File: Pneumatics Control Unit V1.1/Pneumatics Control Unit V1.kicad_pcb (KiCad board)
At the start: 4 copper layers, 53.6 x 65.4 mm, 80 parts, among them J1 TX_PORT, J10 Conn_01x02_Male, J11 Conn_01x02_Male, J12 10118194-0001LF, J13 Conn_01x03_Male, J14 Conn_01x03_Male, J2 RX_PORT, J3 MICROMOD-2222, J4 Conn_01x02_Male, J5 Conn_01x02_Male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

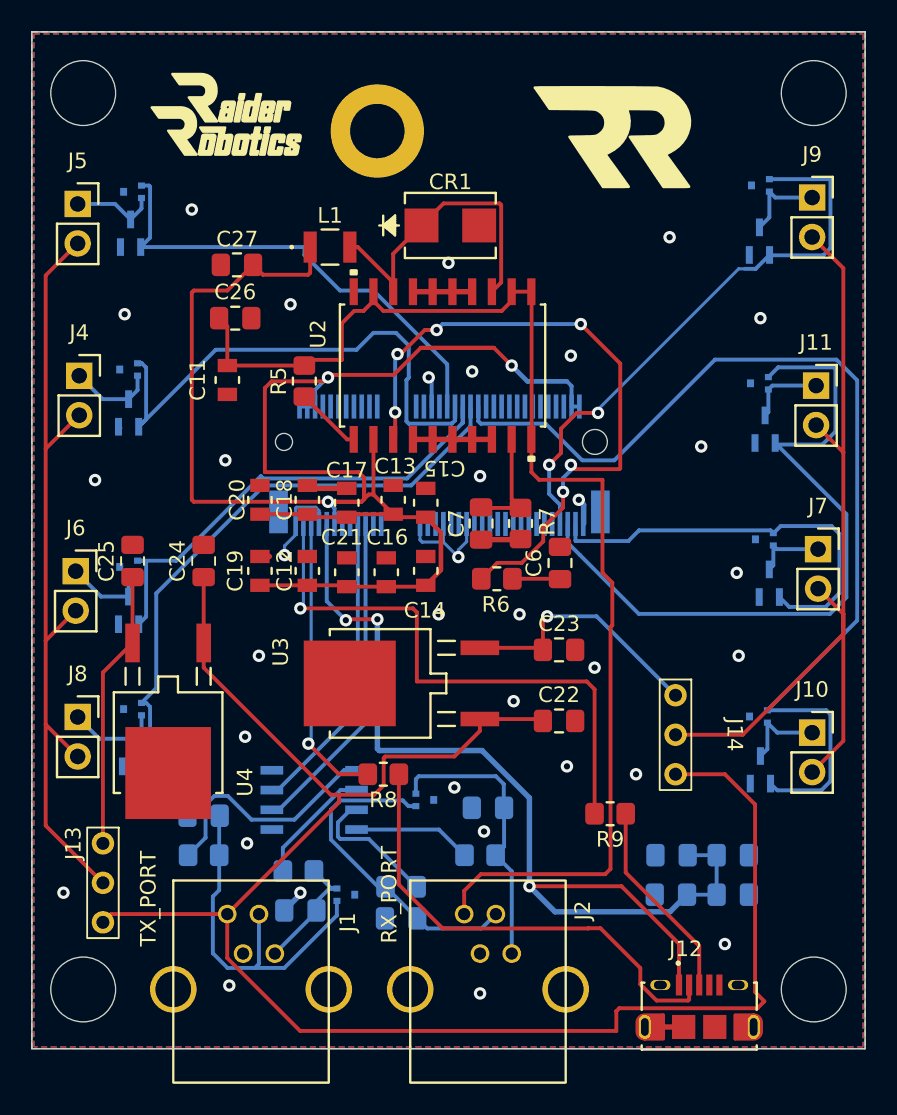
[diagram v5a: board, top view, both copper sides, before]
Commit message: Fixing some smaller issues
Removed isolated zones. Fixed some error classes
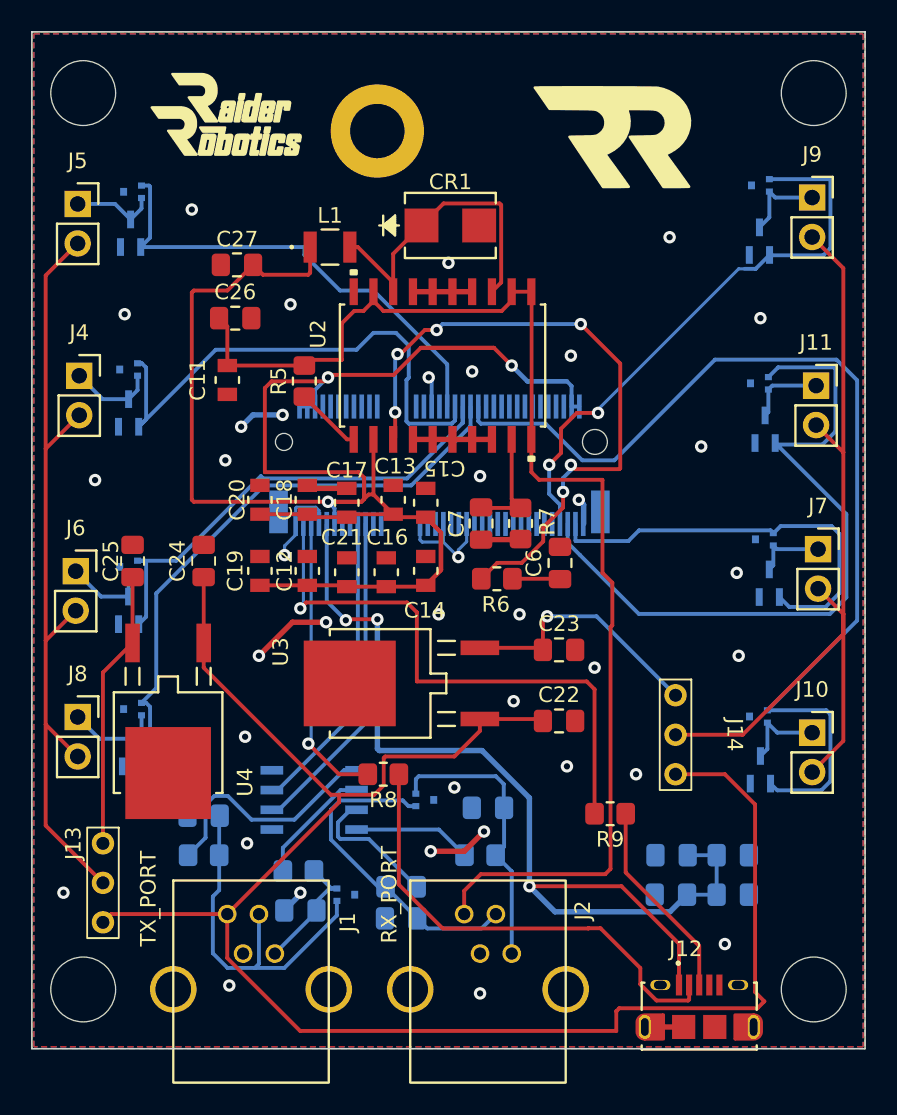
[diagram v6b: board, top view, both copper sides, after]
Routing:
- net GND: track 36.9 -> 47.2 mm, vias 34 -> 38
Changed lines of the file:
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@@
     (property "ki_keywords" "cap capacitor")
     (attr smd)
-    (fp_text reference "C25" (at 0 -1.68 90) (layer "F.SilkS")
+    (fp_text reference "C25" (at 0 -1.397 90) (layer "F.SilkS")
         (effects (font (size 1 1) (thickness 0.15)))
     )
@@
       (stroke (width 0.1) (type solid)) (fill none) (layer "F.Fab"))
     (pad "1" smd rect locked (at -1.3 -2.7) (size 0.4 1.35) (layers "F.Cu" "F.Paste" "F.Mask")
-      (net 78 "Net-(J12-Pad1)") (pinfunction "1") (pintype "passive"))
+      (net 78 "Net-(J12-Pad1)") (pinfunction "1") (pintype "passive") (clearance 0.2))
     (pad "2" smd rect locked (at -0.65 -2.7) (size 0.4 1.35) (layers "F.Cu" "F.Paste" "F.Mask")
       (net 76 "Net-(J12-Pad2)") (pinfunction "2") (pintype "passive"))
@@
     (fp_arc (start 3.225 1.9) (mid 2.625 2.5) (end 2.025 1.9)
       (stroke (width 0.1) (type solid)) (layer "B.Fab"))
-    (fp_arc (start 10.4 3) (mid 10.065332 2.842295) (end 9.925 2.5)
+    (fp_arc (start 10.4 3) (mid 10.065368 2.842287) (end 9.925 2.5)
       (stroke (width 0.1) (type solid)) (layer "B.Fab"))
     (fp_arc (start 10.4 3) (mid 10.819368 3.180631) (end 10.999999 3.599999)
@@
   (segment (start 115.808 120.61) (end 115.808 118.364) (width 0.25) (layer "B.Cu") (net 1))
   (segment (start 115.401489 121.016511) (end 115.401489 124.672489) (width 0.25) (layer "B.Cu") (net 1))
+  (segment (start 131.572 118.11) (end 129.413 118.11) (width 0.35) (layer "F.Cu") (net 2))
   (segment (start 130.81 91.6178) (end 129.54 91.6178) (width 0.35) (layer "F.Cu") (net 2))
   (segment (start 145.685 129.413) (end 143.185 129.413) (width 0.35) (layer "F.Cu") (net 2))
-  (segment (start 132.461 98.256) (end 132.6515 98.0655) (width 0.35) (layer "F.Cu") (net 2))
   (segment (start 130.81 82.1182) (end 132.08 82.1182) (width 0.35) (layer "F.Cu") (net 2))
   (segment (start 132.6515 98.0655) (end 135.154 98.0655) (width 0.35) (layer "F.Cu") (net 2))
+  (segment (start 122.682 103.378) (end 120.523 103.378) (width 0.35) (layer "F.Cu") (net 2))
   (segment (start 121.666 94.7667) (end 121.4755 94.5762) (width 0.35) (layer "F.Cu") (net 2))
   (segment (start 130.81 82.1182) (end 129.54 82.1182) (width 0.35) (layer "F.Cu") (net 2))
-  (segment (start 129.0073 99.2364) (end 129.0955 99.1482) (width 0.35) (layer "F.Cu") (net 2))
   (segment (start 128.27 91.6178) (end 129.54 91.6178) (width 0.35) (layer "F.Cu") (net 2))
-  (segment (start 118.4275 99.1482) (end 119.0378 99.1482) (width 0.35) (layer "F.Cu") (net 2))
   (segment (start 135.154 98.0655) (end 135.1915 98.028) (width 0.35) (layer "F.Cu") (net 2))
+  (segment (start 132.842 116.84) (end 131.572 118.11) (width 0.35) (layer "F.Cu") (net 2))
   (segment (start 124.0155 94.7667) (end 121.666 94.7667) (width 0.35) (layer "F.Cu") (net 2))
+  (segment (start 120.523 103.378) (end 118.364 105.537) (width 0.35) (layer "F.Cu") (net 2))
   (segment (start 132.08 91.6178) (end 130.81 91.6178) (width 0.35) (layer "F.Cu") (net 2))
   (segment (start 129.54 82.1182) (end 128.27 82.1182) (width 0.35) (layer "F.Cu") (net 2))
@@
   (via (at 129.286 87.63) (size 0.8) (drill 0.4) (layers "F.Cu" "B.Cu") (net 2))
   (via (at 118.364 105.537) (size 0.8) (drill 0.4) (layers "F.Cu" "B.Cu") (free) (net 2))
+  (via (at 122.682 103.378) (size 0.8) (drill 0.4) (layers "F.Cu" "B.Cu") (free) (net 2))
   (via (at 144.78 78.613) (size 0.8) (drill 0.4) (layers "F.Cu" "B.Cu") (free) (net 2))
   (via (at 149.225 105.537) (size 0.8) (drill 0.4) (layers "F.Cu" "B.Cu") (free) (net 2))
@@
   (via (at 134.747 108.458) (size 0.8) (drill 0.4) (layers "F.Cu" "B.Cu") (free) (net 2))
   (via (at 132.08 87.249) (size 0.8) (drill 0.4) (layers "F.Cu" "B.Cu") (free) (net 2))
+  (via (at 129.413 118.11) (size 0.8) (drill 0.4) (layers "F.Cu" "B.Cu") (free) (net 2))
   (via (at 129.921 102.87) (size 0.8) (drill 0.4) (layers "F.Cu" "B.Cu") (free) (net 2))
   (via (at 130.937 114.0085) (size 0.8) (drill 0.4) (layers "F.Cu" "B.Cu") (net 2))
+  (via (at 117.221 90.805) (size 0.8) (drill 0.4) (layers "F.Cu" "B.Cu") (free) (net 2))
   (via (at 149.098 100.203) (size 0.8) (drill 0.4) (layers "F.Cu" "B.Cu") (net 2))
   (via (at 148.336 124.079) (size 0.8) (drill 0.4) (layers "F.Cu" "B.Cu") (free) (net 2))
@@
   (via (at 132.588 127.254) (size 0.8) (drill 0.4) (layers "F.Cu" "B.Cu") (free) (net 2))
   (via (at 117.475 110.744) (size 0.8) (drill 0.4) (layers "F.Cu" "B.Cu") (free) (net 2))
+  (via (at 119.888 90.043) (size 0.8) (drill 0.4) (layers "F.Cu" "B.Cu") (free) (net 2))
   (via (at 132.588 93.98) (size 0.8) (drill 0.4) (layers "F.Cu" "B.Cu") (free) (net 2))
   (via (at 135.128 102.87) (size 0.8) (drill 0.4) (layers "F.Cu" "B.Cu") (free) (net 2))
@@
   (segment (start 129.4755 87.8195) (end 129.4755 89.50625) (width 0.25) (layer "B.Cu") (net 2))
   (segment (start 131.191 99.187) (end 130.2255 98.2215) (width 0.2) (layer "B.Cu") (net 2))
-  (segment (start 109.407 90.878498) (end 109.332001 90.803499) (width 0.35) (layer "B.Cu") (net 2))
   (segment (start 128.7255 98.080272) (end 128.866728 98.2215) (width 0.2) (layer "B.Cu") (net 2))
   (segment (start 120.015 98.465772) (end 120.7255 97.755272) (width 0.2) (layer "B.Cu") (net 2))
@@
   (segment (start 122.016739 95.981739) (end 122.2255 96.1905) (width 0.2) (layer "B.Cu") (net 2))
   (segment (start 120.7255 97.755272) (end 120.7255 97.05625) (width 0.2) (layer "B.Cu") (net 2))
-  (segment (start 109.586001 112.647499) (end 109.586001 112.990199) (width 0.35) (layer "B.Cu") (net 2))
   (segment (start 128.866728 98.2215) (end 130.2255 98.2215) (width 0.2) (layer "B.Cu") (net 2))
-  (segment (start 109.407 79.2985) (end 109.459001 79.246499) (width 0.35) (layer "B.Cu") (net 2))
   (segment (start 131.7255 98.1975) (end 131.7255 97.05625) (width 0.2) (layer "B.Cu") (net 2))
-  (segment (start 109.332001 91.171001) (end 109.332001 90.803499) (width 0.35) (layer "B.Cu") (net 2))
+  (segment (start 119.888 90.043) (end 117.983 90.043) (width 0.35) (layer "B.Cu") (net 2))
   (segment (start 120.015 99.06) (end 120.015 98.465772) (width 0.2) (layer "B.Cu") (net 2))
   (segment (start 139.250011 95.816011) (end 139.250011 97.05625) (width 0.35) (layer "B.Cu") (net 2))
   (segment (start 130.2255 98.2215) (end 130.2255 97.05625) (width 0.2) (layer "B.Cu") (net 2))
+  (segment (start 117.983 90.043) (end 117.221 90.805) (width 0.35) (layer "B.Cu") (net 2))
   (segment (start 131.191 99.187) (end 131.191 98.732) (width 0.2) (layer "B.Cu") (net 2))
   (segment (start 121.031 120.8825) (end 119.9935 121.92) (width 0.35) (layer "B.Cu") (net 2))
@@
   (segment (start 128.524 107.188) (end 128.524 102.743) (width 0.25) (layer "F.Cu") (net 23))
   (segment (start 139.954 107.696) (end 139.446 107.188) (width 0.25) (layer "F.Cu") (net 23))
-  (segment (start 128.27 102.489) (end 121.026 102.489) (width 0.25) (layer "F.Cu") (net 23))
-  (segment (start 139.446 107.188) (end 128.524 107.188) (width 0.25) (layer "F.Cu") (net 23))
-  (segment (start 128.524 102.743) (end 128.27 102.489) (width 0.25) (layer "F.Cu") (net 23))
+  (segment (start 128.524 102.743) (end 127.889 102.108) (width 0.25) (layer "F.Cu") (net 23))
   (segment (start 139.954 115.697) (end 139.954 107.696) (width 0.25) (layer "F.Cu") (net 23))
+  (segment (start 139.446 107.188) (end 128.524 107.188) (width 0.25) (layer "F.Cu") (net 23))
+  (segment (start 121.407 102.108) (end 121.026 102.489) (width 0.25) (layer "F.Cu") (net 23))
+  (segment (start 127.889 102.108) (end 121.407 102.108) (width 0.25) (layer "F.Cu") (net 23))
   (via (at 121.026 102.489) (size 0.8) (drill 0.4) (layers "F.Cu" "B.Cu") (net 23))
   (segment (start 121.2255 97.05625) (end 121.2255 102.2895) (width 0.2) (layer "B.Cu") (net 23))
@@
   (segment (start 116.326 122.152) (end 116.326 124.979457) (width 0.25) (layer "F.Cu") (net 66))
   (segment (start 116.326 122.152) (end 108.861 122.152) (width 0.25) (layer "F.Cu") (net 66))
-  (segment (start 114.812 100.4825) (end 114.808 100.4785) (width 0.25) (layer "F.Cu") (net 66))
   (segment (start 130.937 112.014) (end 132.5753 110.3757) (width 0.25) (layer "F.Cu") (net 66))
   (segment (start 122.9855 114.4765) (end 123.5215 114.4765) (width 0.25) (layer "F.Cu") (net 66))
@@
   (segment (start 141.53952 128.20848) (end 150.42952 128.20848) (width 0.25) (layer "F.Cu") (net 66))
   (segment (start 148.336 113.157) (end 145.161 113.157) (width 0.25) (layer "F.Cu") (net 66))
-  (segment (start 114.812 100.5333) (end 114.808 100.5293) (width 0.25) (layer "F.Cu") (net 66))
   (segment (start 126.39048 113.865684) (end 126.39048 112.11552) (width 0.25) (layer "F.Cu") (net 66))
   (segment (start 108.861 122.152) (end 108.331 122.682) (width 0.25) (layer "F.Cu") (net 66))
@@
   (segment (start 136.906 102.997) (end 140.081 102.997) (width 0.25) (layer "B.Cu") (net 87))
   (segment (start 140.081 102.997) (end 145.161 108.077) (width 0.25) (layer "B.Cu") (net 87))
-  (segment (start 110.232 100.4825) (end 110.236 100.4785) (width 0.25) (layer "F.Cu") (net 88))
   (segment (start 108.331 106.6125) (end 108.331 117.602) (width 0.25) (layer "F.Cu") (net 88))
   (segment (start 110.232 104.7115) (end 108.331 106.6125) (width 0.25) (layer "F.Cu") (net 88))
   (segment (start 110.232 104.7115) (end 110.232 100.4825) (width 0.25) (layer "F.Cu") (net 88))
-  (segment (start 110.232 100.5333) (end 110.236 100.5293) (width 0.25) (layer "F.Cu") (net 88))
   (zone (net 2) (net_name "GND") (layers F&B.Cu) (hatch edge 0.508)
     (connect_pads (clearance 0.508))

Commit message: Adding inner ground planes. This baby grounded now
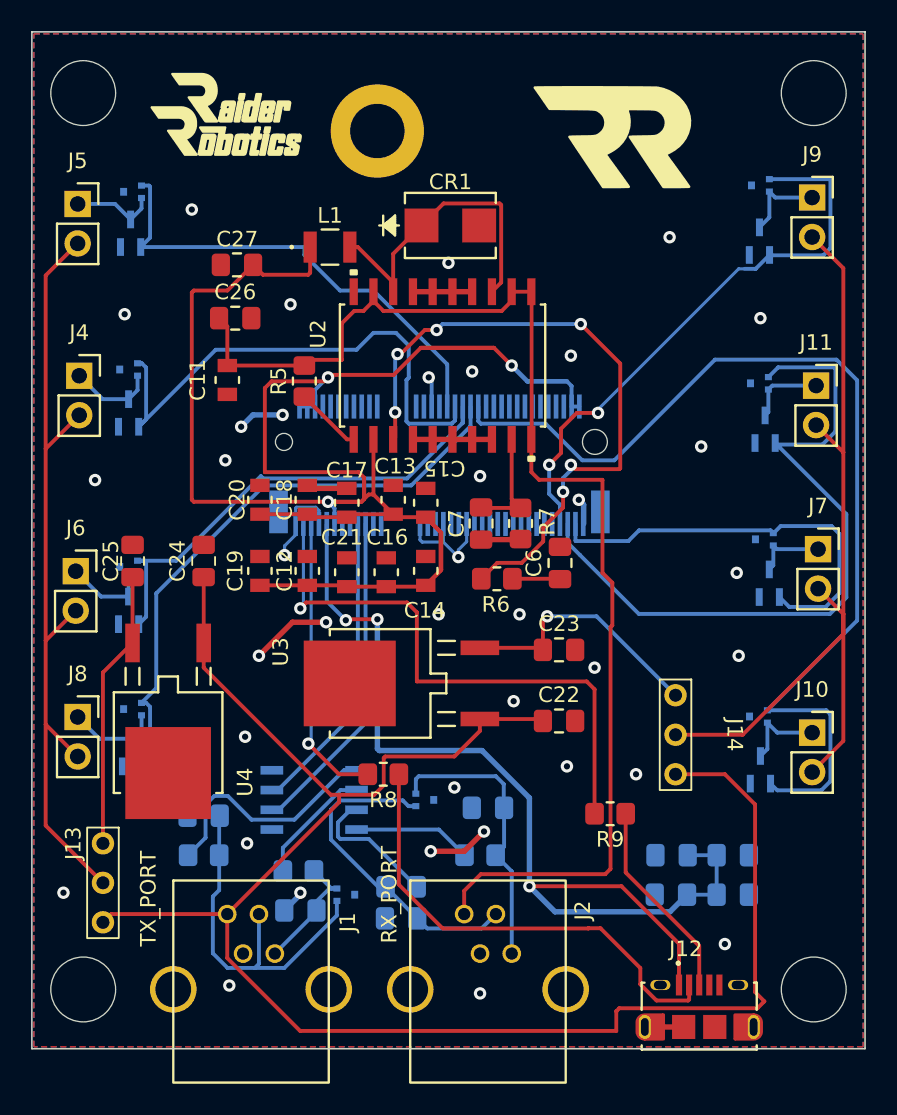
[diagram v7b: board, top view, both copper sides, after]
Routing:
- added copper zone on In1.Cu, net GND
- added copper zone on In2.Cu, net GND
- removed copper zone on In1.Cu, net (none)
- removed copper zone on In2.Cu, net (none)
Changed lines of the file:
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@@
       (drillshape 0)
       (scaleselection 1)
-      (outputdirectory "C:/Users/caboo/Documents/GitHub/pcb-design/Pneumatics Control Unit V1.1/Gerber Files/")
+      (outputdirectory "../../../PCBs/Gen1/")
     )
   )
@@
     (fp_arc (start 3.225 1.9) (mid 2.625 2.5) (end 2.025 1.9)
       (stroke (width 0.1) (type solid)) (layer "B.Fab"))
-    (fp_arc (start 10.4 3) (mid 10.065368 2.842287) (end 9.925 2.5)
+    (fp_arc (start 10.4 3) (mid 10.065332 2.842295) (end 9.925 2.5)
       (stroke (width 0.1) (type solid)) (layer "B.Fab"))
     (fp_arc (start 10.4 3) (mid 10.819368 3.180631) (end 10.999999 3.599999)
@@
     )
   )
-  (zone (net 2) (net_name "GND") (layers F&B.Cu) (hatch edge 0.508)
+  (zone (net 2) (net_name "GND") (layers "In1.Cu" "In2.Cu") (hatch edge 0.508)
     (connect_pads (clearance 0.508))
     (min_thickness 0.254) (filled_areas_thickness no)
@@
     )
   )
-  (zone (net 0) (net_name "") (layers "In1.Cu" "In2.Cu") (hatch edge 0.508)
+  (zone (net 2) (net_name "GND") (layers "In1.Cu" "In2.Cu") (hatch edge 0.508)
     (connect_pads (clearance 0.508))
     (min_thickness 0.254) (filled_areas_thickness no)
